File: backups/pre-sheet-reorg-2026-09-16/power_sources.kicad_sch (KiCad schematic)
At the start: 24 parts, among them J3 ESC pads (CURR TX M4 M3 M2 M1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, J4 USB_C_PROGRAM_POWER, U25 TPS2121RUXR, U26 AP63205WU-7

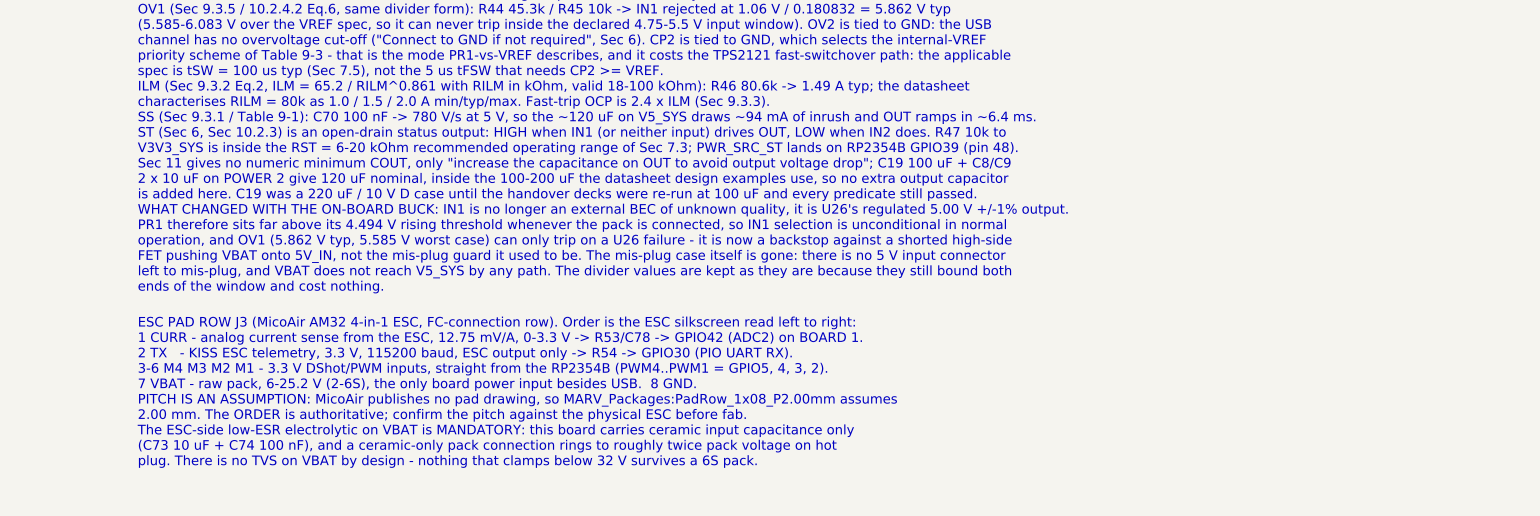
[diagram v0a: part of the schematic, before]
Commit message: Schematic re-organised into 11 per-subsystem pages, drawn as wired blocks
Each subsystem now has its own sheet (RP2354B, USB/debug, ICM-45686, BMP581,
ADXL375, microSD, QSPI expansion, VBAT buck + ESC row, priority mux, 3.3 V
rail, IO block) with the IC's own decoupling, pull-ups, test points and
connectors placed beside it and wired, labels only for nets leaving the
block. Root sheet is an index. tools/build_power.py grows a small layout
engine (wire routing, junctions, decoupling ladders, note flow) with
self-checks for dangling wires and multi-net wire islands; the long design
notes are preserved verbatim as module constants.

Purely presentational: netlist fingerprint (tools/netlist_fingerprint.py,
new) is identical before and after, ERC 0, power checks pass. PCB footprint
paths re-pointed at the new sheet UUIDs by tools/relink_pcb_paths.py (new);
the board diff is path lines only, DRC unconnected count unchanged.
README/DESIGN_SPEC sheet lists updated; pre-change sheets and generator in
backups/pre-sheet-reorg-2026-09-16/.

Also carries the uncommitted work that preceded it: PCB routing, plane
stitching and route-analysis tools (tools/route_*.py, stitch_planes.py),
GPIO remap in PINOUT.md / check_power_netlist.py / setup_pcb.py, and the
grommet mounting-hole footprint update.

Co-Authored-By: Claude Fable 5.1 <noreply@anthropic.com>
Claude-Session: https://claude.ai/code/session_01Y51PayhRcgfdi3hVsfn4qg
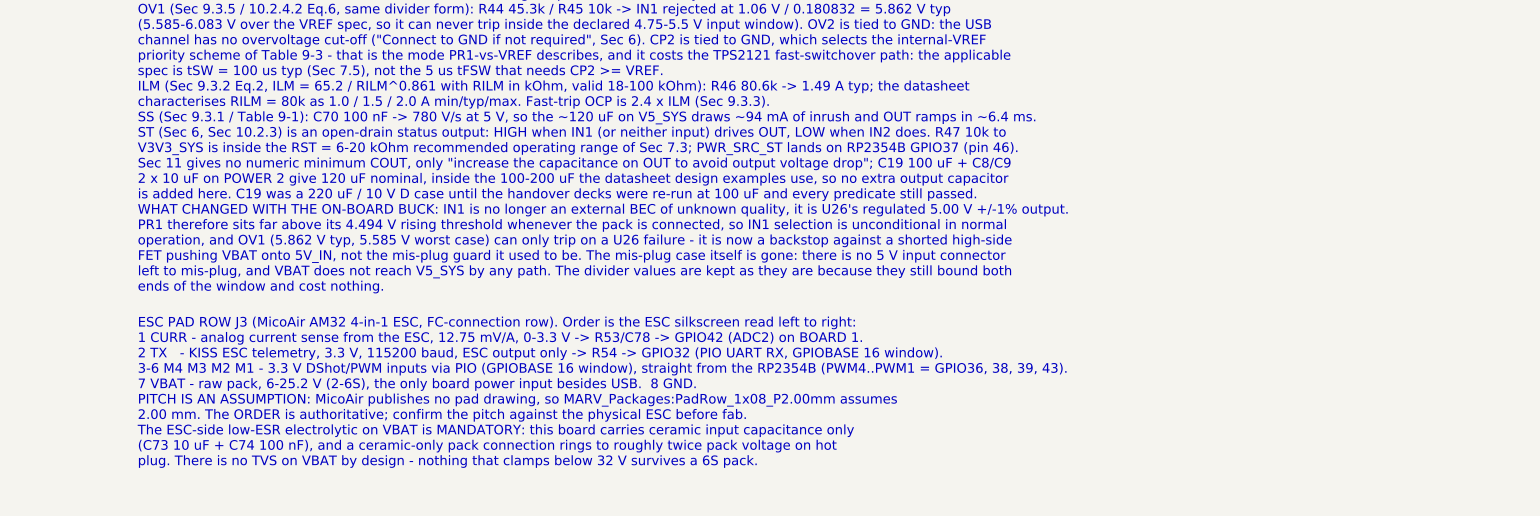
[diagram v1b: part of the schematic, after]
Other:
- note added: "ESC PAD ROW J3 (MicoAir AM32 4-in-1 ESC, FC-connection row). Order is the ESC silkscreen read left to right: 1 CURR - analog current sense from the ESC, 12.75 mV/A, 0-3.3 V -> R53/C78 -> GPIO42 (ADC2) on BOARD 1. 2 TX - KISS ESC telemetry, 3.3 V, 115200 baud, ESC output only -> R54 -> GPIO32 (PIO UART RX, GPIOBASE 16 window). 3-6 M4 M3 M2 M1 - 3.3 V DShot/PWM inputs via PIO (GPIOBASE 16 window), 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"
- note removed: "ESC PAD ROW J3 (MicoAir AM32 4-in-1 ESC, FC-connection row). Order is the ESC silkscreen read left to right: 1 CURR - analog current sense from the ESC, 12.75 mV/A, 0-3.3 V -> R53/C78 -> GPIO42 (ADC2) on BOARD 1. 2 TX - KISS ESC telemetry, 3.3 V, 115200 baud, ESC output only -> R54 -> GPIO30 (PIO UART RX). 3-6 M4 M3 M2 M1 - 3.3 V DShot/PWM inputs, straight from the RP2354B (PWM4..PWM1 = GPIO5, 4,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"
